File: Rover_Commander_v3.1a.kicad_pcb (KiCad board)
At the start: 2 copper layers, 77 x 42 mm, 73 parts, among them Q1 Crystal KX-7 25MHz, Q2 Crystal KX-7 25MHz, U1 RTL8201CP, U2 L7805ABD2T-TR, U3 H1102NLT, U4 LD1117S33TR_SOT223, U5 STM32F107RCTx, U6 TJA1040T, U7 M95160-WMN6TP

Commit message: asd1
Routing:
- net GND: track 432.1 -> 437.6 mm
- net /+3V3_EEPROM: track 111.7 -> 109.5 mm
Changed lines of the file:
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@@
     (thickness 1.6)
     (drawings 42)
-    (tracks 1012)
+    (tracks 1018)
     (zones 0)
     (modules 73)
@@
     (mod_text_size 1 1)
     (mod_text_width 0.15)
-    (pad_size 1 0.25)
+    (pad_size 1.3 0.25)
     (pad_drill 0)
     (pad_to_mask_clearance 0.2)
@@
   (segment (start 140.97 86.868) (end 142.22 86.868) (width 0.25) (layer B.Cu) (net 1))
   (segment (start 142.22 86.868) (end 147.32 86.868) (width 0.25) (layer B.Cu) (net 1))
+  (segment (start 135.414 96.23) (end 133.414 96.23) (width 0.1) (layer B.Cu) (net 2))
+  (segment (start 147.828 82.0358) (end 147.828 81.7756) (width 0.1) (layer B.Cu) (net 2))
+  (segment (start 147.4501 81.772333) (end 147.4501 81.6579) (width 0.1) (layer F.Cu) (net 2))
+  (segment (start 145.288 80.4) (end 145.288 82.296) (width 0.1) (layer F.Cu) (net 2))
+  (segment (start 145.288 82.296) (end 145.796 82.296) (width 0.1) (layer F.Cu) (net 2))
+  (segment (start 145.796 82.296) (end 146.299451 81.792549) (width 0.1) (layer F.Cu) (net 2))
+  (segment (start 145.288 80.4) (end 133.604 80.4) (width 0.5) (layer F.Cu) (net 2))
+  (segment (start 152.908 80.4) (end 145.288 80.4) (width 0.5) (layer F.Cu) (net 2))
   (segment (start 137.434 83.82) (end 137.434 84.57) (width 0.25) (layer B.Cu) (net 2))
   (segment (start 137.434 84.57) (end 135.136 86.868) (width 0.25) (layer B.Cu) (net 2))
@@
   (segment (start 151.384 121.092) (end 150.876 121.6) (width 0.3) (layer F.Cu) (net 2))
   (segment (start 161.6 80.4) (end 152.908 80.4) (width 0.5) (layer F.Cu) (net 2))
-  (segment (start 152.908 80.4) (end 133.604 80.4) (width 0.5) (layer F.Cu) (net 2))
   (segment (start 152.908 82.296) (end 152.908 80.4) (width 0.3) (layer F.Cu) (net 2))
   (segment (start 128.016 87.376) (end 128.016 85.344) (width 0.3) (layer F.Cu) (net 2))
@@
   (segment (start 138.208 98.486) (end 134.070001 98.486) (width 0.25) (layer B.Cu) (net 14))
   (segment (start 134.070001 98.486) (end 133.814 98.33) (width 0.25) (layer B.Cu) (net 14))
+  (segment (start 136.444001 96.73) (end 135.414 96.73) (width 0.25) (layer B.Cu) (net 15))
   (segment (start 139.7 100.584) (end 139.7 99.784) (width 0.2) (layer B.Cu) (net 15))
   (segment (start 139.7 99.784) (end 139.192 99.276) (width 0.2) (layer B.Cu) (net 15))
@@
   (segment (start 138.208 96.586) (end 136.688002 96.586) (width 0.25) (layer B.Cu) (net 15))
   (segment (start 136.688002 96.586) (end 136.444001 96.73) (width 0.25) (layer B.Cu) (net 15))
-  (segment (start 136.444001 96.73) (end 135.414 96.73) (width 0.25) (layer B.Cu) (net 15))
   (segment (start 144.306002 91.474002) (end 143.746999 90.914999) (width 0.25) (layer B.Cu) (net 16))
   (segment (start 137.752001 90.914999) (end 137.668 90.999) (width 0.25) (layer B.Cu) (net 16))
@@
   (segment (start 132.682 114.937) (end 134.867 114.937) (width 0.5) (layer B.Cu) (net 74))
   (segment (start 134.867 114.937) (end 134.952 114.852) (width 0.5) (layer B.Cu) (net 74))
+  (segment (start 150.368 82.128) (end 149.818 82.128) (width 0.3) (layer F.Cu) (net 75))
+  (segment (start 149.818 82.128) (end 148.738723 83.207277) (width 0.3) (layer F.Cu) (net 75))
+  (segment (start 148.738723 83.207277) (end 141.836723 83.207277) (width 0.3) (layer F.Cu) (net 75))
+  (segment (start 150.368 82.128) (end 150.368 82.278) (width 0.3) (layer F.Cu) (net 75))
+  (segment (start 150.368 82.278) (end 152.286 84.196) (width 0.3) (layer F.Cu) (net 75))
+  (segment (start 152.286 84.196) (end 152.433 84.196) (width 0.1) (layer F.Cu) (net 75))
+  (segment (start 152.433 84.196) (end 152.908 84.196) (width 0.1) (layer F.Cu) (net 75))
+  (segment (start 141.836723 83.207277) (end 136.652 88.392) (width 0.3) (layer F.Cu) (net 75))
   (segment (start 159.93 115.824) (end 161.454 114.3) (width 0.3) (layer B.Cu) (net 75))
   (segment (start 161.454 114.3) (end 175.3 114.3) (width 0.3) (layer B.Cu) (net 75))
@@
   (segment (start 136.652 88.392) (end 135.414 89.63) (width 0.3) (layer B.Cu) (net 75))
   (segment (start 135.414 89.63) (end 133.939001 89.63) (width 0.3) (layer B.Cu) (net 75))
-  (segment (start 150.368 82.128) (end 150.368 82.278) (width 0.3) (layer F.Cu) (net 75))
-  (segment (start 150.368 82.278) (end 151.318001 83.228001) (width 0.3) (layer F.Cu) (net 75))
-  (segment (start 151.318001 83.228001) (end 151.318001 83.327999) (width 0.3) (layer F.Cu) (net 75))
-  (segment (start 141.816001 83.227999) (end 136.652 88.392) (width 0.3) (layer F.Cu) (net 75))
-  (segment (start 151.318001 83.327999) (end 151.218001 83.227999) (width 0.3) (layer F.Cu) (net 75))
   (via (at 136.652 88.392) (size 0.6) (drill 0.4) (layers F.Cu B.Cu) (net 75))
-  (segment (start 151.218001 83.227999) (end 141.816001 83.227999) (width 0.3) (layer F.Cu) (net 75))
   (segment (start 134.952 117.152) (end 141.252 117.152) (width 0.3) (layer B.Cu) (net 75))
   (segment (start 133.534515 99.982864) (end 133.510864 99.982864) (width 0.15) (layer B.Cu) (net 75))
@@
   (segment (start 152.908 84.196) (end 155.992 84.196) (width 0.3) (layer F.Cu) (net 75))
   (segment (start 155.992 84.196) (end 156.464 84.668) (width 0.3) (layer F.Cu) (net 75))
-  (segment (start 150.368 82.128) (end 150.368 82.331) (width 0.3) (layer F.Cu) (net 75))
-  (segment (start 150.368 82.331) (end 152.233 84.196) (width 0.3) (layer F.Cu) (net 75))
-  (segment (start 152.233 84.196) (end 152.908 84.196) (width 0.3) (layer F.Cu) (net 75))
   (segment (start 137.668 115.316) (end 137.668 116.332) (width 0.3) (layer B.Cu) (net 75))
   (segment (start 137.668 116.332) (end 136.848 117.152) (width 0.3) (layer B.Cu) (net 75))

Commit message: finish tracing
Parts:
- moved R23 3.08 mm to (144.0, 104.6)
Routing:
- net GND: track 437.6 -> 485.7 mm, vias 12 -> 13
- net /+3V3_STM: track 33.4 -> 79.9 mm, vias 4 -> 7
- net /+3V3_EEPROM: track 109.5 -> 149.8 mm, vias 5 -> 9
- net /+5V: track 93.5 -> 105.7 mm
- net Net-(U5-Pad49): track 68.8 -> 63.8 mm
- net Net-(R23-Pad1): track 39.2 -> 43.6 mm
- net /BUZZER: track 7.10 -> 11.0 mm
- net Net-(R18-Pad1): track 21.2 -> 24.0 mm
- net /ETH_MDC: track 49.6 -> 52.3 mm
- net /ETH_MII_TX_CLK: track 27.3 -> 29.8 mm
- net /ETH_MII_RX_ER: track 25.4 -> 27.8 mm
- net /EEPROM_CS: track 15.8 -> 18.2 mm
- net /ETH_MII_TXD2: track 27.4 -> 29.6 mm
- net /ADC_Vbat: track 51.2 -> 53.1 mm
- net /ETH_MII_CRS: track 42.7 -> 44.6 mm
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
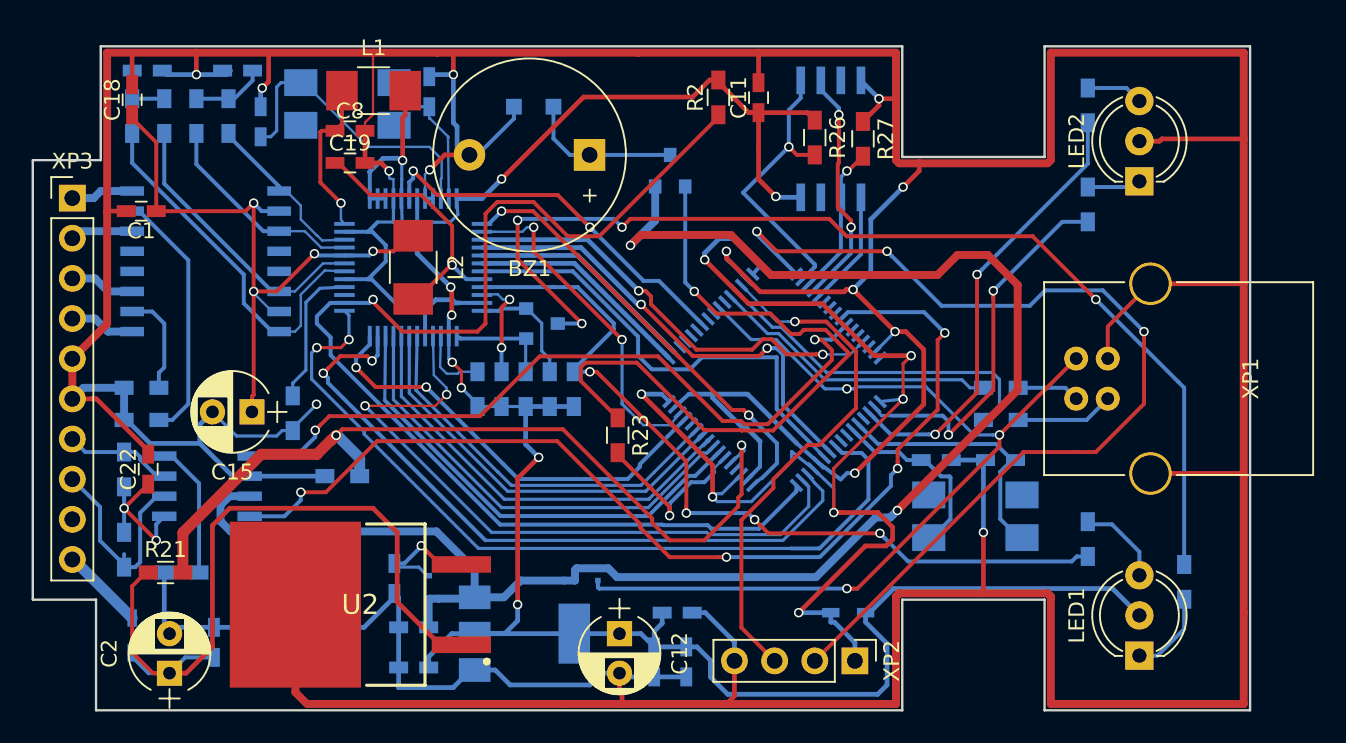
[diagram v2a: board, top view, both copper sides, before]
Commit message: add OBD@ connecters labels on front silk layer
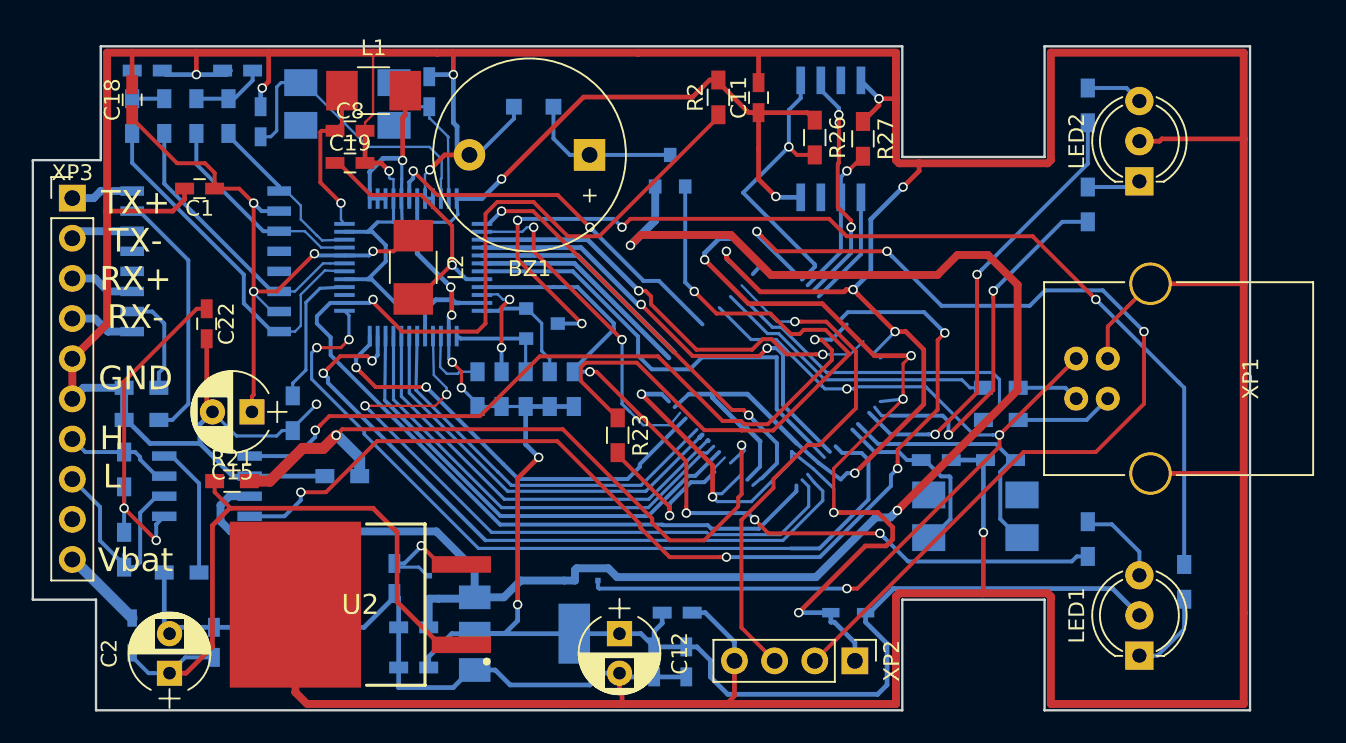
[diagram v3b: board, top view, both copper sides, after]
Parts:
- removed U5: STM32F107RCTx, Housings_QFP:LQFP-64_10x10mm_Pitch0.5mm
- moved C22 9.91 mm to (118.0, 97.5), turned to 270 degrees
- moved R21 7.15 mm to (119.6, 107.5)
- moved C1 3.96 mm to (117.5, 89.0)
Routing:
- net Net-(C22-Pad1): track 11.0 -> 24.0 mm
- net /ADC_Vbat: track 53.1 -> 45.0 mm
- net /STM_ADC_12V: track 48.2 -> 41.8 mm
- net GND: track 485.7 -> 488.8 mm
- net /TRANS_CT: track 42.0 -> 39.6 mm
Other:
- board text added: "GND"
- board text added: "H L"
- board text added: "TX+ TX- RX+ RX-"
- board text added: "Vbat"

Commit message: fix missing arm, fill layer with GND
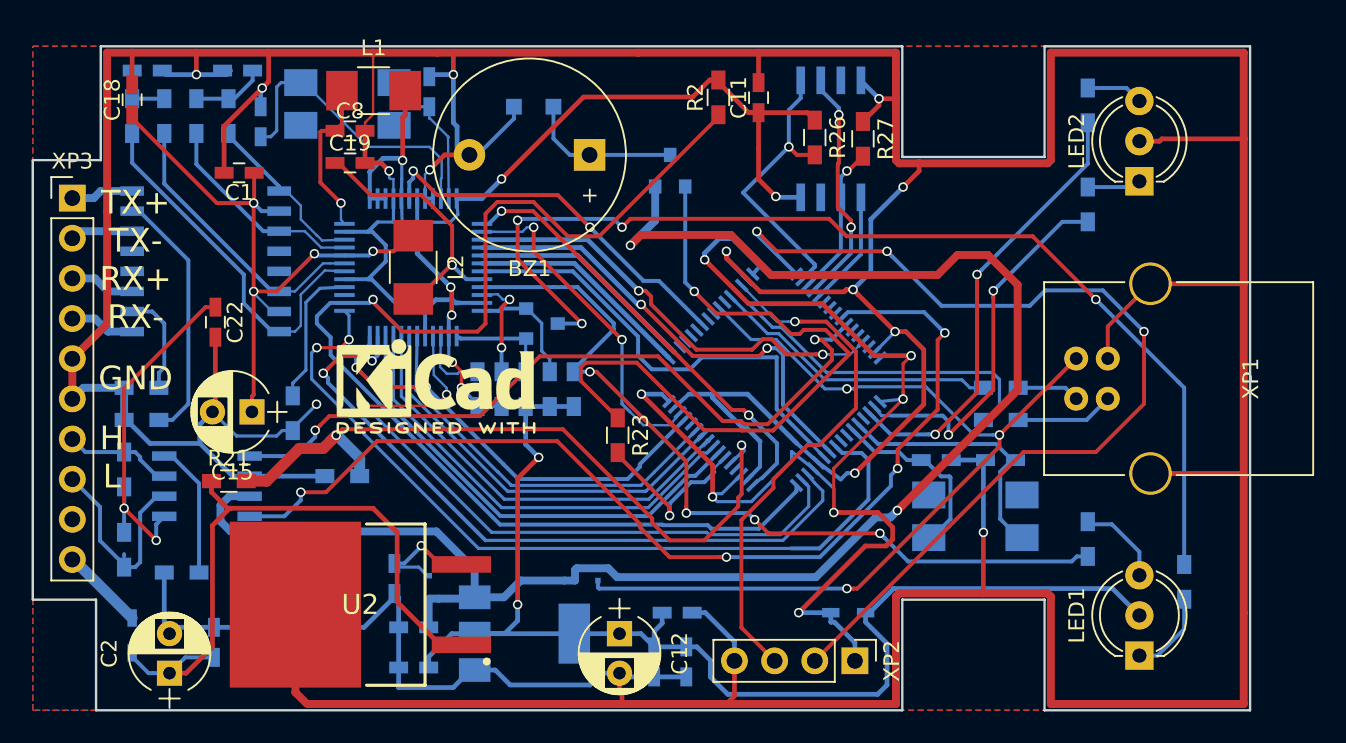
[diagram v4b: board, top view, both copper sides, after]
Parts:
- added REF***: KiCad-Logo2_6mm_SilkScreen, Symbols:KiCad-Logo2_6mm_SilkScreen, F.Cu at (132.5, 101.5)
- added U5: STM32F107RCTx, Housings_QFP:LQFP-64_10x10mm_Pitch0.5mm, B.Cu at (153.9, 101.1)
- moved C1 2.69 mm to (120.0, 88.0)
- moved C22 0.56 mm to (118.5, 97.5)
- moved R21 0.20 mm to (119.4, 107.5)
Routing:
- net /TRANS_CT: track 39.6 -> 41.0 mm
- net GND: track 488.8 -> 489.3 mm
- added copper zone on B.Cu, net GND
- added copper zone on F.Cu, net GND
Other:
- board text removed: "Vbat"

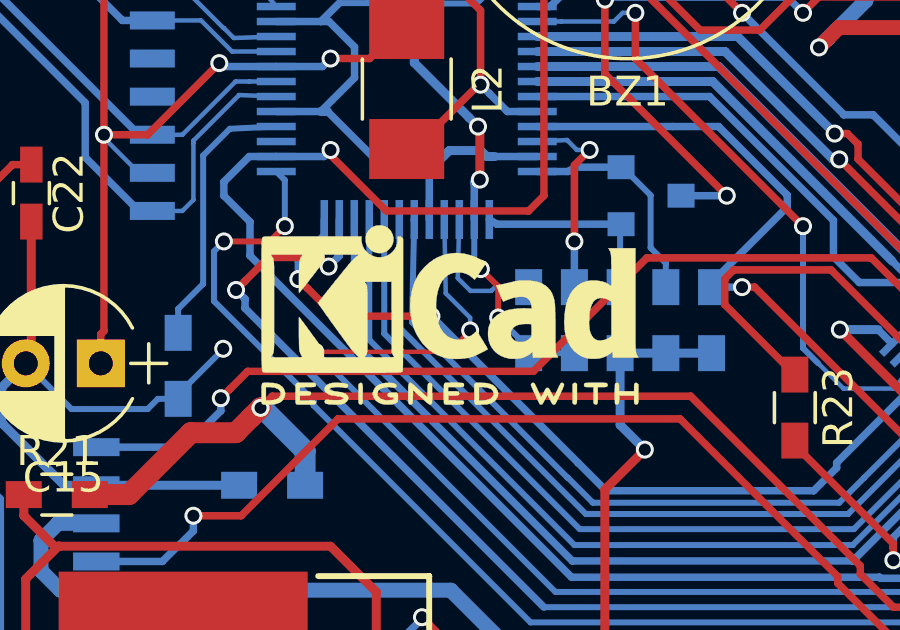
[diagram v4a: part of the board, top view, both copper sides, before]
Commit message: delete KICAD label
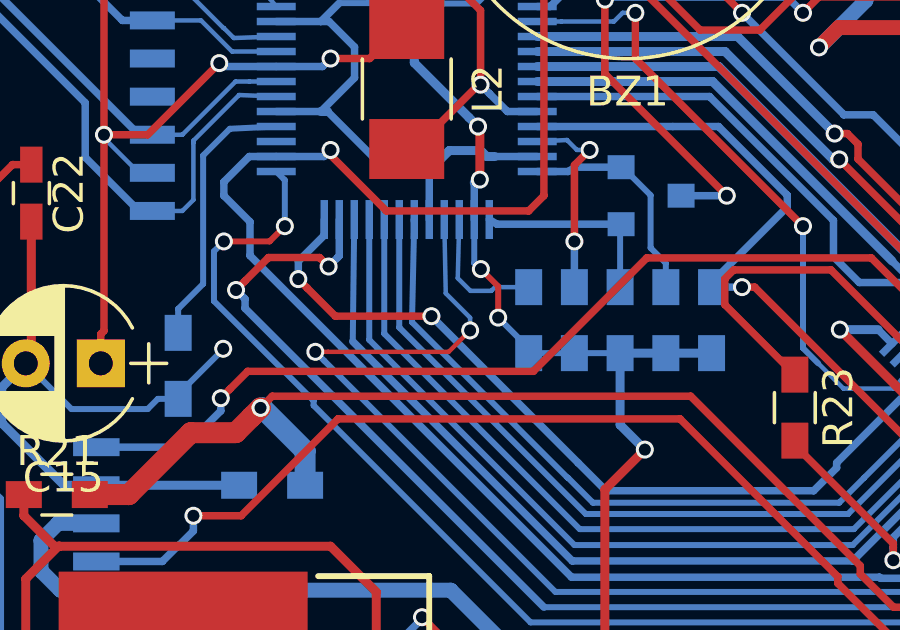
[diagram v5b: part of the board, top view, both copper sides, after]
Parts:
- removed REF***: KiCad-Logo2_6mm_SilkScreen, Symbols:KiCad-Logo2_6mm_SilkScreen

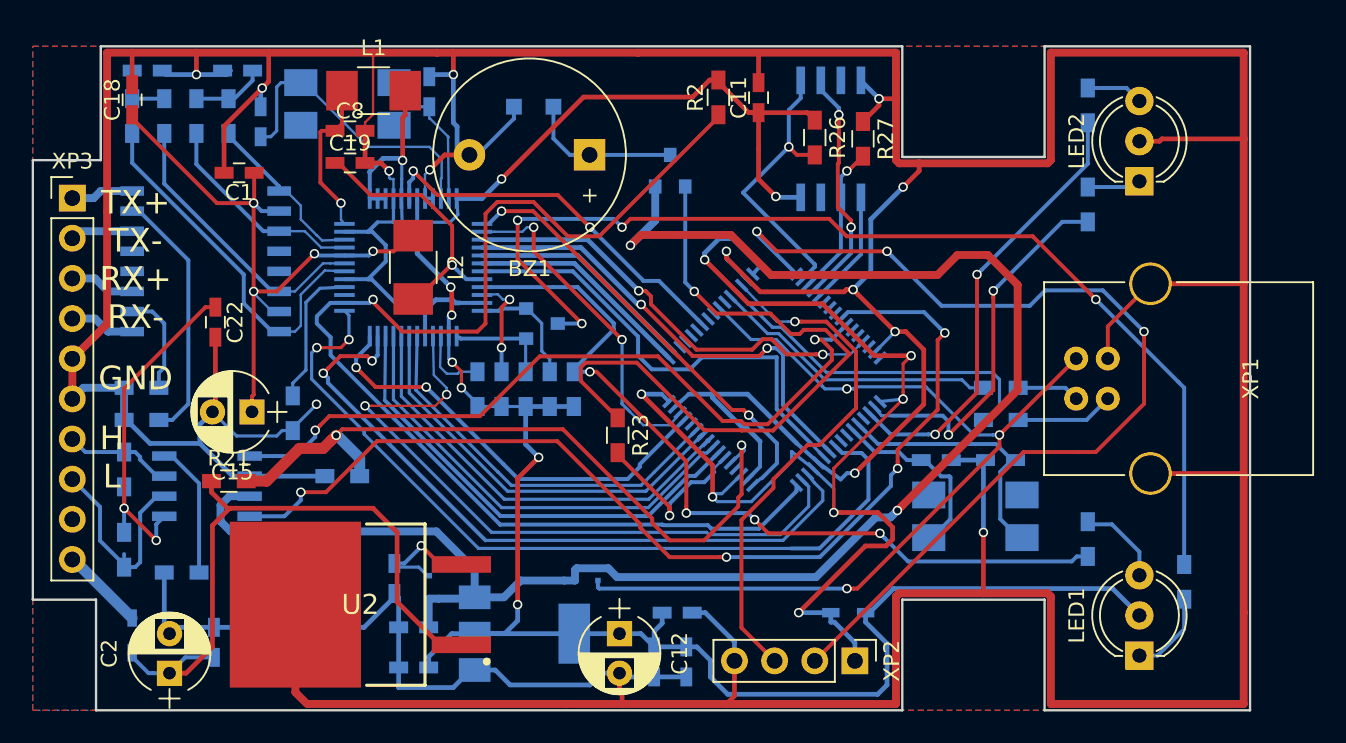
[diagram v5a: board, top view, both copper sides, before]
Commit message: fix silk layer and some DRC errors
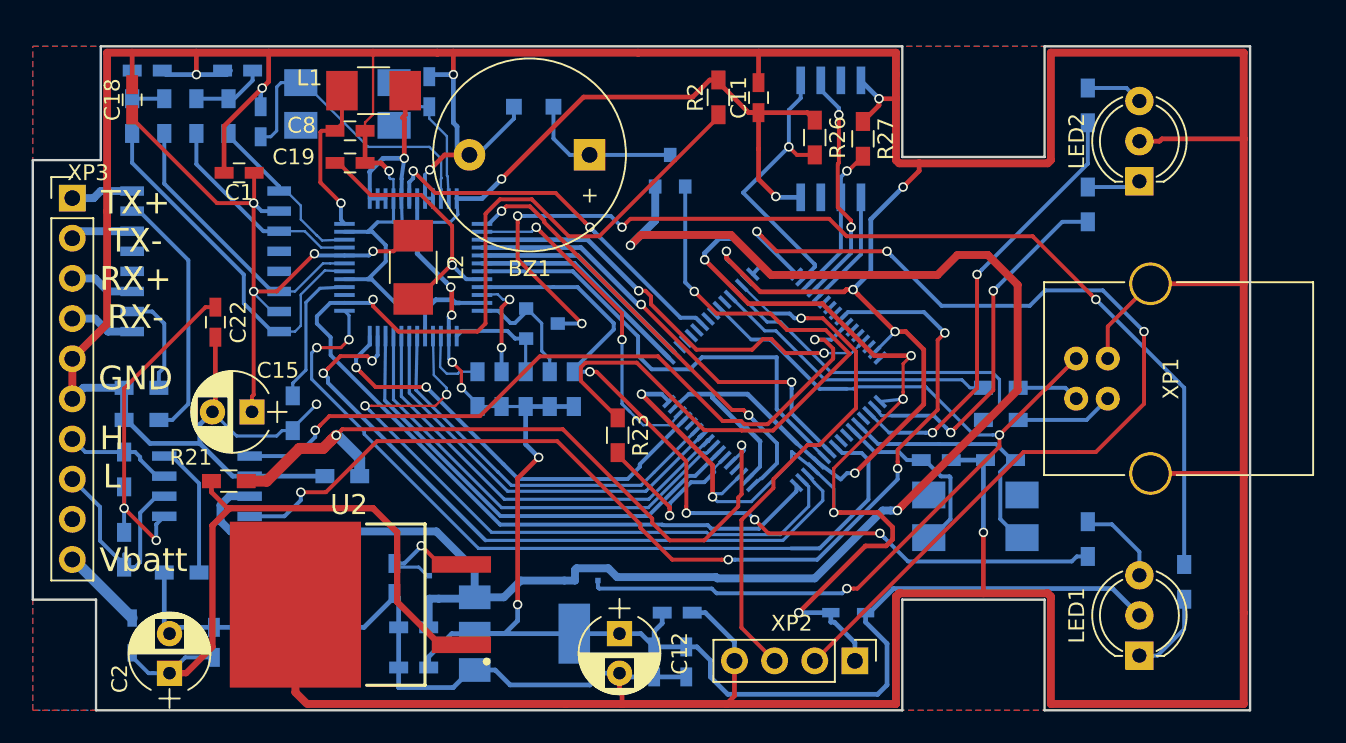
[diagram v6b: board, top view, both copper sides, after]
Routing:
- net /ETH_MII_TXD2: track 29.6 -> 28.5 mm
- net Net-(D3-Pad2): track 7.48 -> 8.26 mm
- net Net-(R18-Pad1): track 24.0 -> 23.4 mm
- net /USB_Vbus: track 58.4 -> 58.6 mm, vias 3 -> 2
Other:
- rule trace_min: 0.15 -> 0.102
- rule via_min_size: 0.4 -> 0.3
- board text added: "Vbatt"
